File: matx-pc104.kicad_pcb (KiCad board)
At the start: 2 copper layers, 171.4 x 243.8 mm, 99 parts, among them J1 ATX-24, J10 Fan2, J11 Fan3, J12 HDD_LED, J13 VGA, J14 Ethernet, J15 Keyboard, J16 Mouse, J17 USB, J18 Serial, J19 VGA, J2 PC104-8, J20 VGA_DDC, J21 Ethernet, J22 Keyboard, J23 Mouse, J24 USB, J25 Serial, J3 PC104-16, J4 Bus_ISA_16bit, J5 Bus_ISA_16bit, J6 Bus_ISA_16bit, J7 Bus_ISA_16bit, J8 F_PANEL, J9 Fan1, Q1 2N7000, Q2 2N7000, SW1 Power, SW2 Reset, U1 L7905, U2 555, U3 74HCT138, U4 74HCT688, U5 74HCT574, U6 ATF16V8C, U7 4047, U8 DC56-11GWA

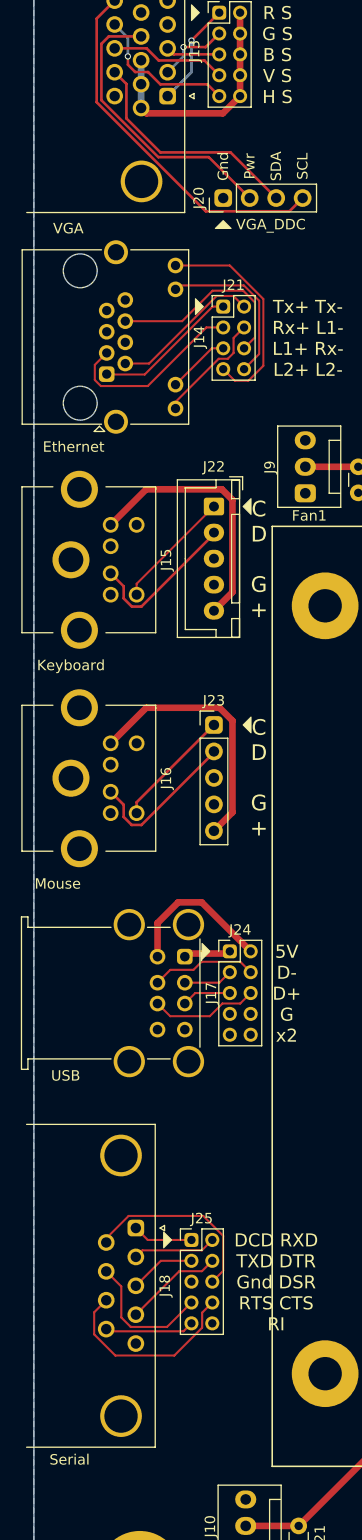
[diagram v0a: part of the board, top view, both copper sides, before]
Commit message: Correct silkscreen - fix VGA pinout, align port labels
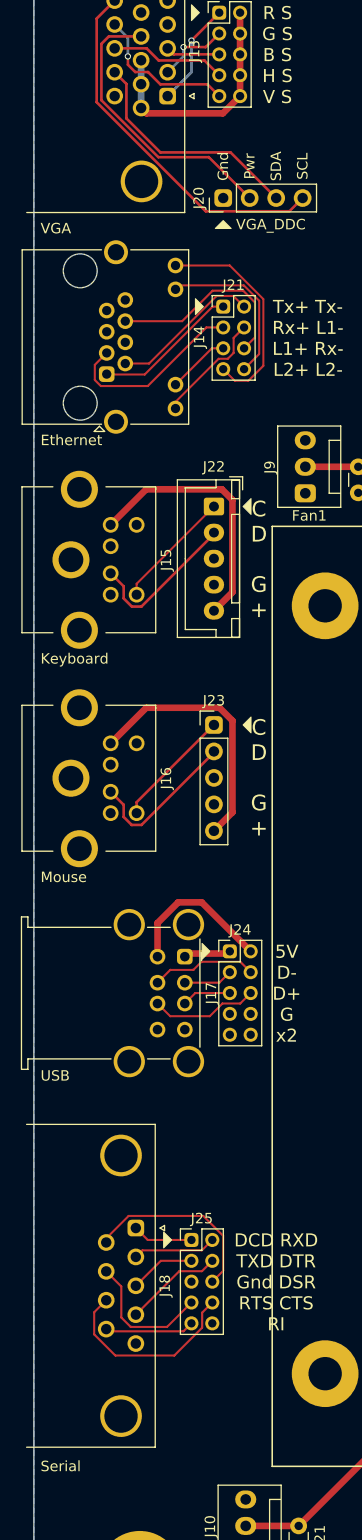
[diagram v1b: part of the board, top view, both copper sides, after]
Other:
- board text added: "R S G S B S H S V S"
- board text removed: "R S G S B S V S H S"
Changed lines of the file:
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@@
       (effects (font (size 1 1) (thickness 0.15)))
     )
-    (fp_text value Serial (at 22.225 6.35 180) (layer F.SilkS)
-      (effects (font (size 1 1) (thickness 0.15)))
+    (fp_text value Serial (at 22.86 9.144 180) (layer F.SilkS)
+      (effects (font (size 1 1) (thickness 0.15)) (justify left))
     )
     (fp_line (start 21.5 -2.35) (end -10.4 -2.35) (layer F.CrtYd) (width 0.05))
@@
       (effects (font (size 1 1) (thickness 0.15)))
     )
-    (fp_text value Mouse (at -11.43 -5.08 180) (layer F.SilkS)
-      (effects (font (size 1 1) (thickness 0.15)))
+    (fp_text value Mouse (at -10.795 -6.731 180) (layer F.SilkS)
+      (effects (font (size 1 1) (thickness 0.15)) (justify left))
     )
     (fp_line (start -8.3 -8.51) (end 5.7 -8.51) (layer F.Fab) (width 0.2))
@@
       (effects (font (size 1 1) (thickness 0.15)))
     )
-    (fp_text value VGA (at 12.7 9.525 180) (layer F.SilkS)
-      (effects (font (size 1 1) (thickness 0.15)))
+    (fp_text value VGA (at 12.7 12.192 180) (layer F.SilkS)
+      (effects (font (size 1 1) (thickness 0.15)) (justify left))
     )
     (fp_line (start -19.74 -1.58) (end -19.74 13.57) (layer F.Fab) (width 0.1))
@@
       (effects (font (size 1 1) (thickness 0.15)))
     )
-    (fp_text value Keyboard (at -11.43 -3.81 180) (layer F.SilkS)
-      (effects (font (size 1 1) (thickness 0.15)))
+    (fp_text value Keyboard (at -10.795 -6.731 180) (layer F.SilkS)
+      (effects (font (size 1 1) (thickness 0.15)) (justify left))
     )
     (fp_line (start -8.3 -8.51) (end 5.7 -8.51) (layer F.Fab) (width 0.2))
@@
       (effects (font (size 1 1) (thickness 0.15)))
     )
-    (fp_text value USB (at 11.43 11.43 180) (layer F.SilkS)
-      (effects (font (size 1 1) (thickness 0.15)))
+    (fp_text value USB (at 11.43 13.843 180) (layer F.SilkS)
+      (effects (font (size 1 1) (thickness 0.15)) (justify left))
     )
     (fp_line (start 12.07 6.17) (end 10.91 7.33) (layer F.CrtYd) (width 0.05))
@@
       (effects (font (size 1 1) (thickness 0.15)))
     )
-    (fp_text value Ethernet (at -6.985 -3.175 180) (layer F.SilkS)
-      (effects (font (size 1 1) (thickness 0.15)))
+    (fp_text value Ethernet (at -6.35 -6.35 180) (layer F.SilkS)
+      (effects (font (size 1 1) (thickness 0.15)) (justify left))
     )
     (fp_line (start -4.695 -7) (end -4.695 7.75) (layer F.Fab) (width 0.1))
@@
   (gr_poly (pts (xy 34.163 53.975) (xy 32.639 53.975) (xy 33.401 53.213)) (layer F.SilkS) (width 0.1))
   (gr_poly (pts (xy 31.115 33.274) (xy 30.353 34.036) (xy 30.353 32.512)) (layer F.SilkS) (width 0.1))
-  (gr_text "R S\nG S\nB S\nV S\nH S" (at 38.608 37.338) (layer F.SilkS)
+  (gr_text "R S\nG S\nB S\nH S\nV S" (at 38.608 37.338) (layer F.SilkS)
     (effects (font (size 1.25 1.25) (thickness 0.2)))
   )

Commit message: Version 1.1. Fix reset issue
Replace reset circuit with passthrough, increase LED decoder cap value, enlarge load resistor footprints, renumber some components
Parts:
- removed the R10 at (178.4, 175.3)
- added J10: RST_IN, Connector_PinHeader_2.54mm:PinHeader_1x02_P2.54mm_Vertical, F.Cu at (180.3, 173.4)
- added REF**: KiCad-Logo_8mm_SilkScreen, Symbol:KiCad-Logo_8mm_SilkScreen, B.Cu at (25.4, 205.7)
- C14: value 0.1uF -> 1uF; footprint Capacitor_THT:C_Disc_D3.0mm_W1.6mm_P2.50mm -> Capacitor_THT:C_Disc_D3.0mm_W2.0mm_P2.50mm
- J9: renamed from J12; value HDD_LED -> HDD_IN
- R12, R13: footprint Resistor_THT:R_Axial_Power_L20.0mm_W6.4mm_P25.40mm -> Resistor_THT:R_Axial_Power_L25.0mm_W6.4mm_P30.48mm
- moved D6 92.5 mm to (127.0, 54.6), turned to 0 degrees
- moved R11 53.8 mm to (127.6, 153.7)
- moved R9 27.9 mm to (176.5, 148.0), turned to 0 degrees
- moved J9 24.2 mm to (180.3, 168.3)
- moved R12 6.98 mm to (170.2, 64.8)
- moved R13 6.98 mm to (180.3, 64.8)
- renumbered J9 to J11, J10 to J12, J11 to J13, J13 to J14, J19 to J15, J20 to J16, J14 to J17, J21 to J18, J15 to J19, J22 to J20, J16 to J21, J23 to J22, J17 to J23, J18 to J25, J25 to J26, R11 to R10, R14 to R11
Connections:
- net /RST_SW renamed /RST_B
- J8 pad 5: /RESET -> /RST_A
- SW2 pad 2: /RESET -> /RST_A
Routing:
- net /L_R: track 3.18 -> 102.0 mm, vias 0 -> 2
- net /RESET: track 241.0 -> 166.4 mm, vias 4 -> 1
- net /RST_A: track 0.00 -> 45.1 mm, vias 0 -> 3
- net +5V: track 1292.5 -> 1278.3 mm
- net /HDD_B: track 9.94 -> 20.0 mm
- net /HDD_A: track 9.94 -> 19.5 mm
- net /PWR_LED: track 15.4 -> 6.13 mm
- net /RST_B: track 47.0 -> 54.9 mm, vias 3 -> 4
- net +12V: track 828.6 -> 821.6 mm
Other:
- board text added: "PD301 1.1 mATX carrier board for PC/104 SBCs"
- board text removed: "Input"
- board text removed: "PD301 1.0 mATX carrier board for PC/104 SBCs"
